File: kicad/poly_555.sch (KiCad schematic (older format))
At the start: 32 parts, among them U1 LM386

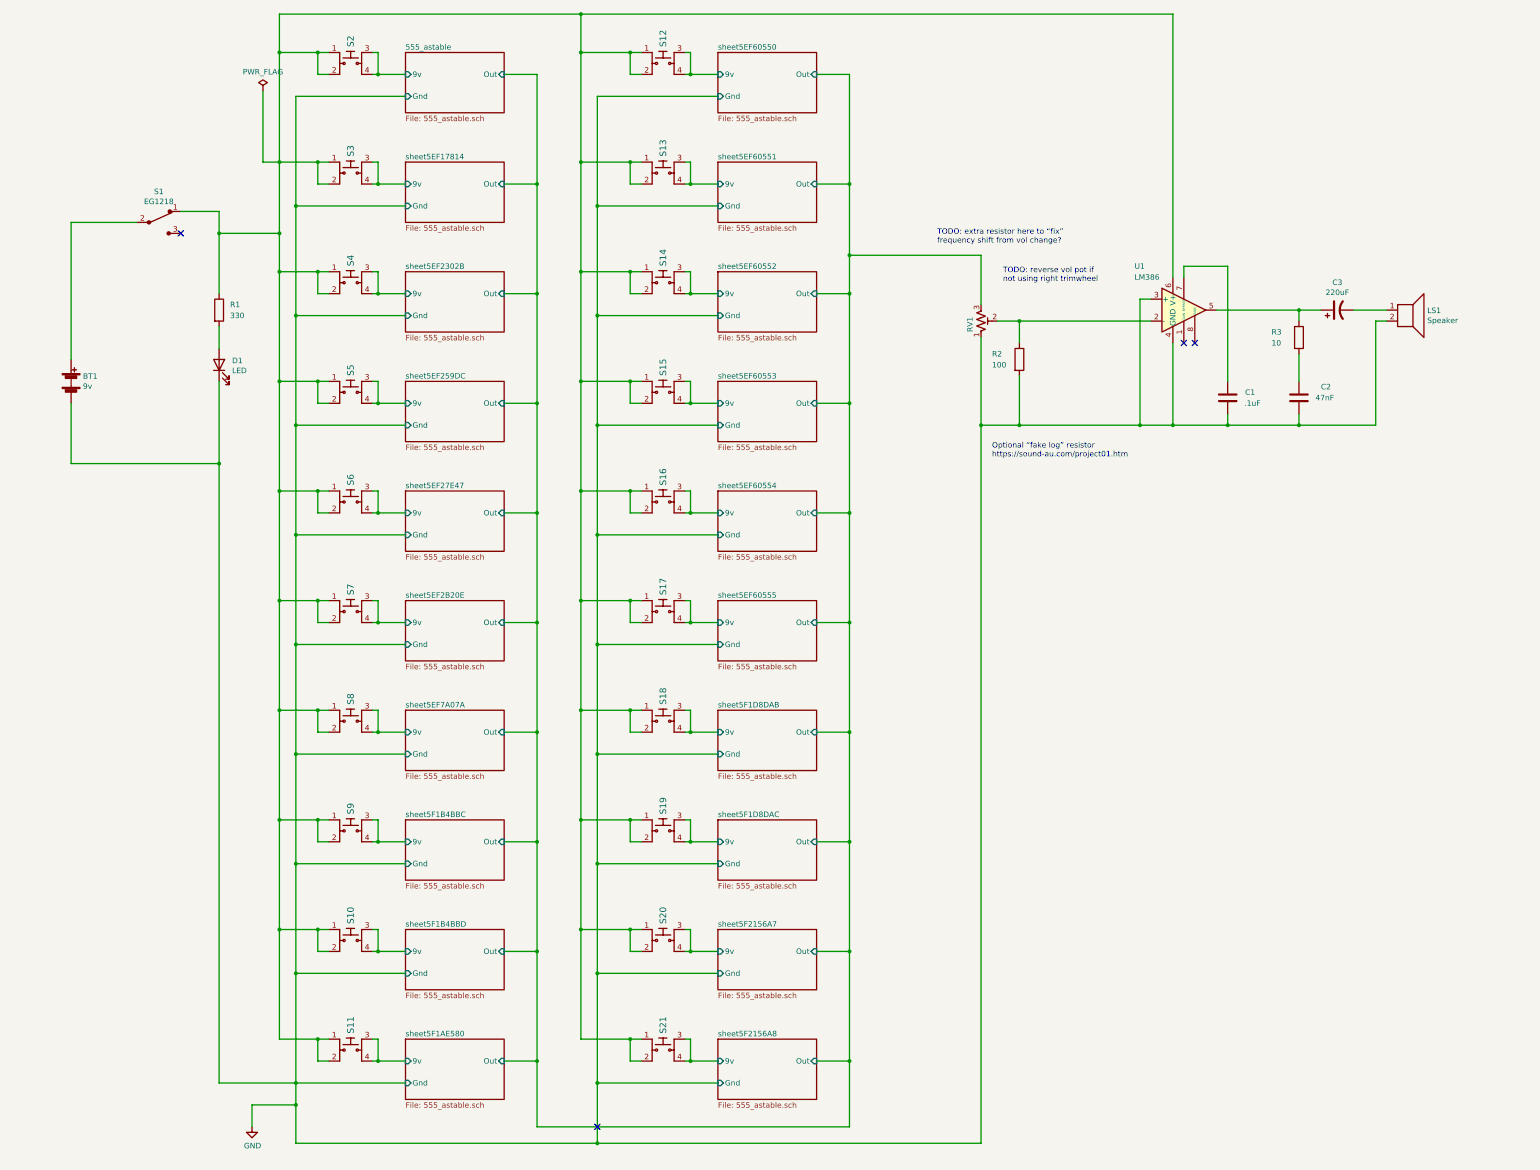
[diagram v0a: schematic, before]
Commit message: Re-annotate to fix key vs 555 mismatch
The alignment of switch to 555 circuit was off, starting around S8. I
believe this was from non-linear copy-pasting when key count jumped from
13 to 20.

No amound of fiddling with the annotation tool seemed to fix and to do
it manually was out of the question, so I ended up deleting 6-20 and
copy-pasting 1-5 three times. I think it worked...
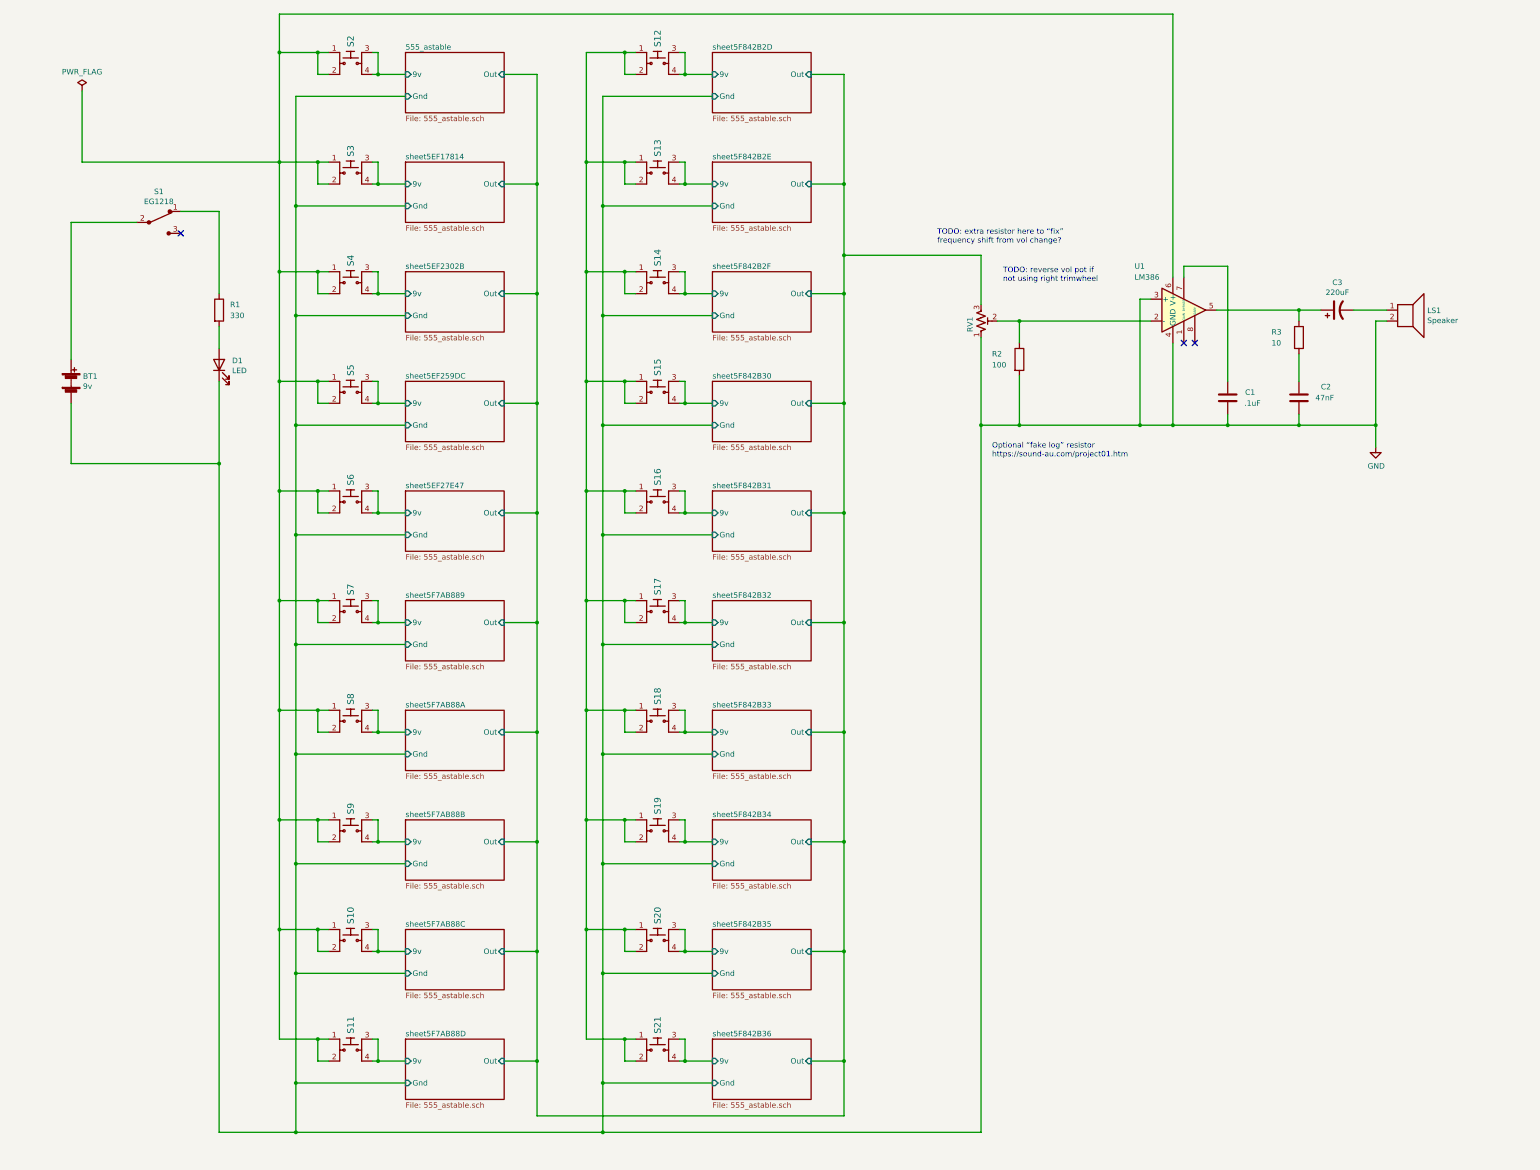
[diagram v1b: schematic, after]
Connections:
- net sheet5EF2B20E/9v renamed sheet5F7AB889/9v
- net sheet5EF60550/9v renamed sheet5F842B2D/9v
- net sheet5EF60551/9v renamed sheet5F842B2E/9v
- net sheet5EF60552/9v renamed sheet5F842B2F/9v
- net sheet5EF60553/9v renamed sheet5F842B30/9v
- net sheet5EF60554/9v renamed sheet5F842B31/9v
- net sheet5EF60555/9v renamed sheet5F842B32/9v
- net sheet5EF7A07A/9v renamed sheet5F7AB88A/9v
- net sheet5F1AE580/9v renamed sheet5F7AB88D/9v
- net sheet5F1B4BBC/9v renamed sheet5F7AB88B/9v
- net sheet5F1B4BBD/9v renamed sheet5F7AB88C/9v
- net sheet5F1D8DAB/9v renamed sheet5F842B33/9v
- net sheet5F1D8DAC/9v renamed sheet5F842B34/9v
- net sheet5F2156A7/9v renamed sheet5F842B35/9v
- net sheet5F2156A8/9v renamed sheet5F842B36/9v
- new net: S10.1, S10.2, S11.1, S11.2, S2.1, S2.2, S3.1, S3.2, S4.1, S4.2, S5.1, S5.2, S6.1, S6.2, S7.1, S7.2, S8.1, S8.2, S9.1, S9.2, U1.6 (V+)
- new net: R1.1, S1.1
- new net: S12.1, S12.2, S13.1, S13.2, S14.1, S14.2, S15.1, S15.2, S16.1, S16.2, S17.1, S17.2, S18.1, S18.2, S19.1, S19.2, S20.1, S20.2, S21.1, S21.2
- no-connect marks 4 -> 3

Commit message: Finish routing
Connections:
- net at S10.1, S10.2, S11.1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: now also R1.1, S1.1, S12.1, S12.2, S13.1, S13.2, S14.1, S14.2, S15.1, S15.2, S16.1, S16.2, S17.1, S17.2, S18.1, S18.2, S19.1, S19.2, S20.1, S20.2, S21.1, S21.2
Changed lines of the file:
@@
 	13100 4650 13100 4450
 Wire Wire Line
-	3100 700  11250 700
+	3100 700  5900 700
 $Sheet
 S 4250 6050 900  550
@@
 	2550 2500 2550 3250
 Wire Wire Line
-	3100 2050 3100 3050
+	3100 2050 3100 2500
 $Sheet
 S 7050 1050 900  550
@@
 Wire Wire Line
 	11250 4450 11750 4450
+Wire Wire Line
+	5900 700  5900 1050
+Connection ~ 5900 700
+Wire Wire Line
+	5900 700  11250 700
+Connection ~ 5900 1050
+Wire Wire Line
+	2550 2500 3100 2500
+Connection ~ 2550 2500
+Connection ~ 3100 2500
+Wire Wire Line
+	3100 2500 3100 3050
 $EndSCHEMATC

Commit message: Start new PCB layout
* wider cavity w/o top
* swap fine trimmer for resistor
* bigger wire holes for speaker,battery
* 5mm LEDs
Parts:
- D1: footprint LED_THT:LED_D3.0mm -> LED_THT:LED_D5.0mm
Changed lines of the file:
@@
 F 0 "D1" V 2589 3782 50  0000 R CNN
 F 1 "LED" V 2498 3782 50  0000 R CNN
-F 2 "LED_THT:LED_D3.0mm" H 2550 3900 50  0001 C CNN
+F 2 "LED_THT:LED_D5.0mm" H 2550 3900 50  0001 C CNN
 F 3 "~" H 2550 3900 50  0001 C CNN
 	1    2550 3900

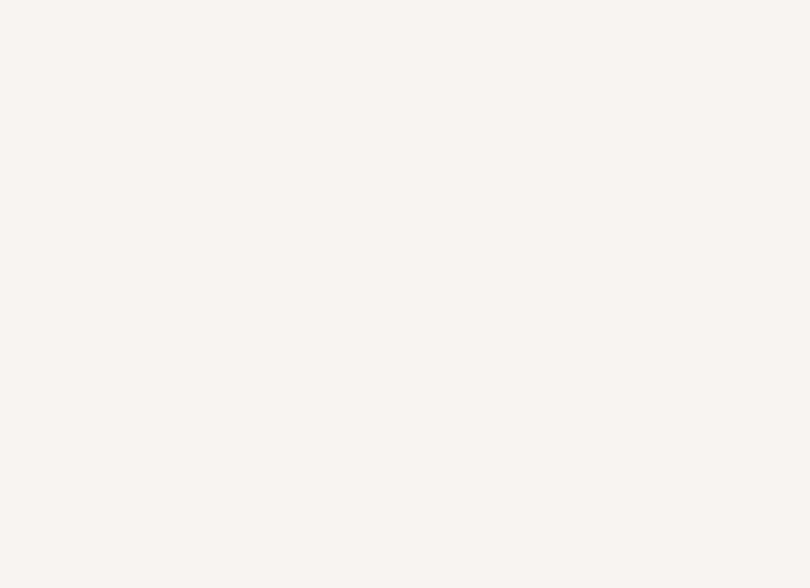
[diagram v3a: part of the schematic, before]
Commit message: Fill negative space with breakoff APC
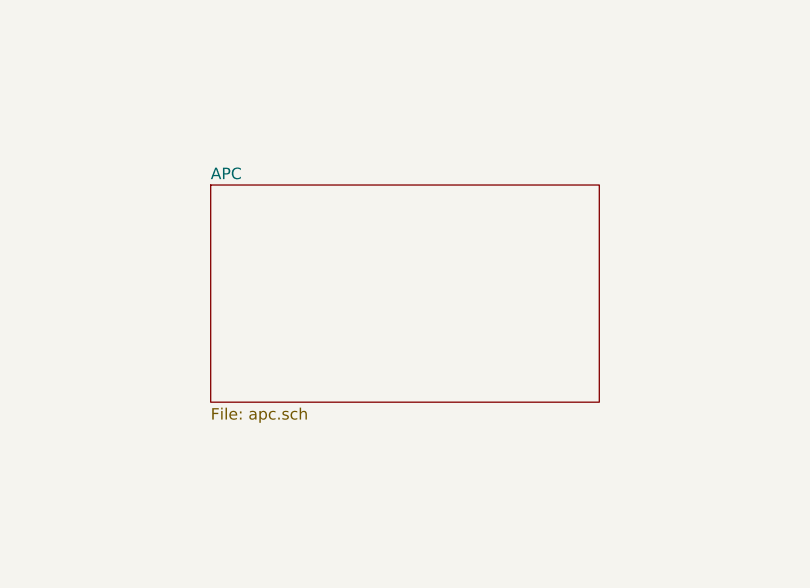
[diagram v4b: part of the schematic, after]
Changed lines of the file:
@@
 $Descr A3 16535 11693
 encoding utf-8
-Sheet 1 21
+Sheet 1 22
 Title ""
 Date ""
@@
 Wire Wire Line
 	3100 2500 3100 3050
+$Sheet
+S 10500 5850 1700 950
+U 5F470266
+F0 "APC" 50
+F1 "apc.sch" 50
+$EndSheet
 $EndSCHEMATC

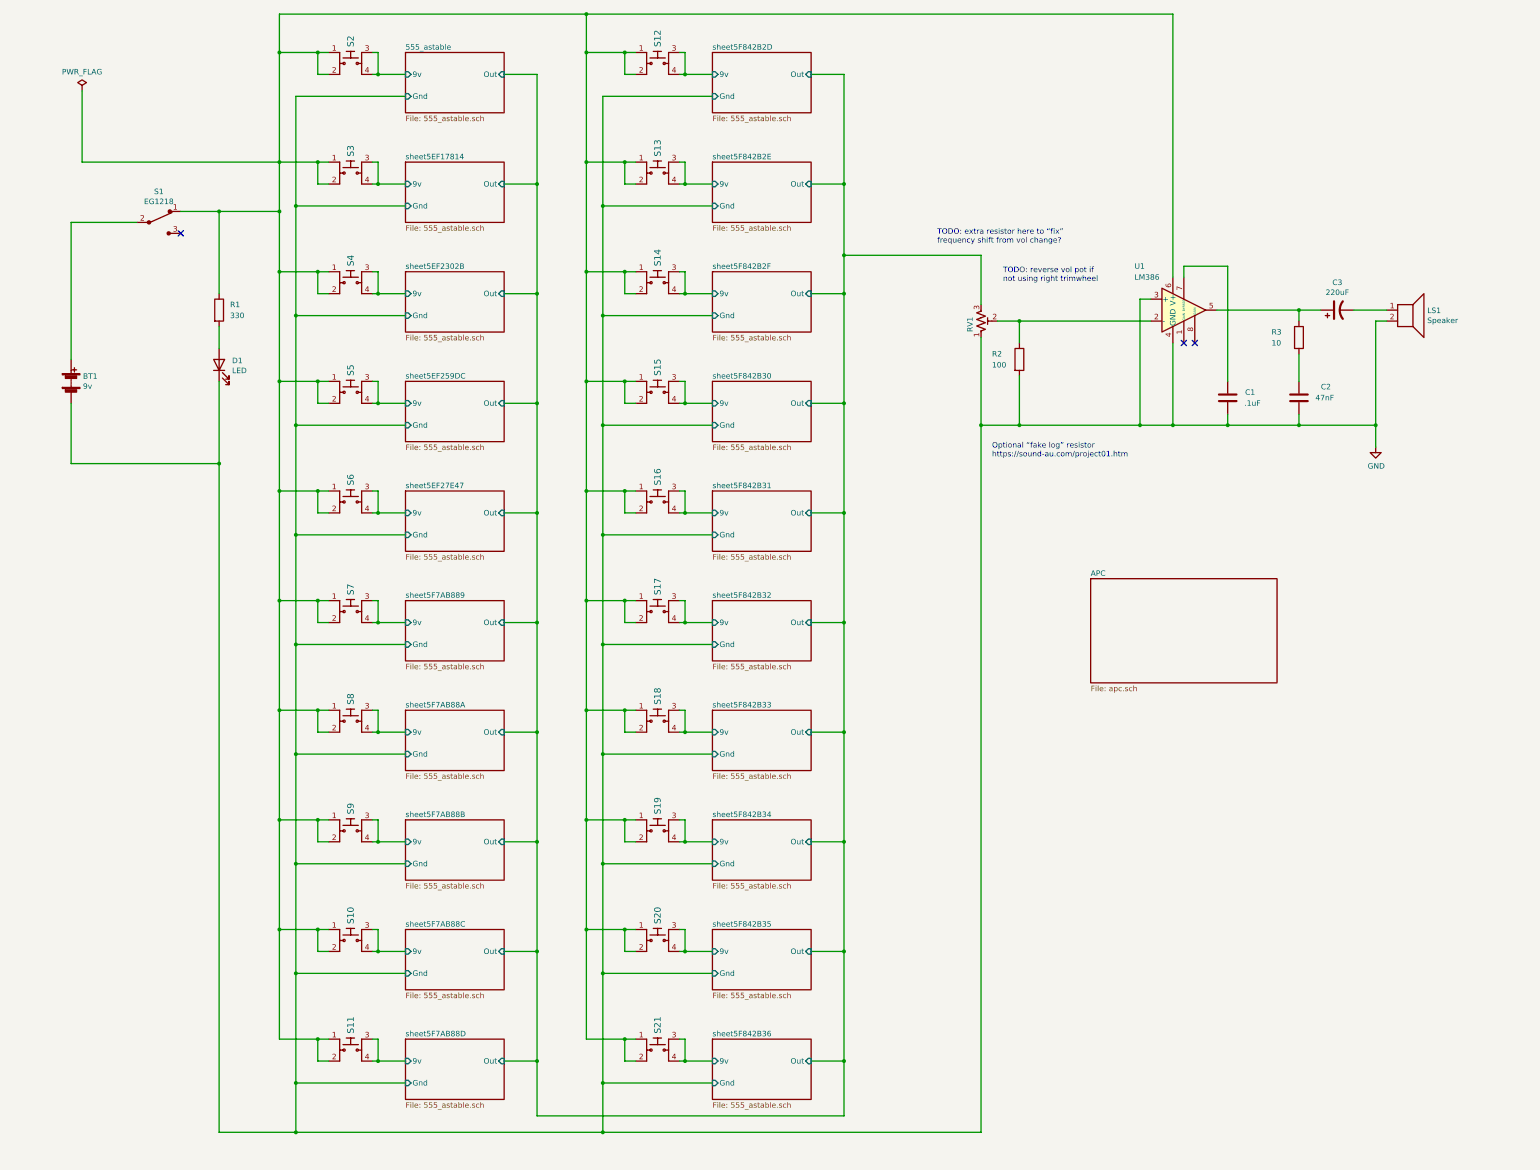
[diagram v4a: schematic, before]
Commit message: PCB revisions:
* Add voltage regulator to POLY_555
* Ditch hitch
* Reorder switches+circuits left to right
* Carve out room for battery
* Mark # 555s
* Label wired pins better

APC updates:

* Fix ground error
* Reverse volume pot direction
* Swap timing cap footprint
* Add stress relief hole for battery wires
* Widen speaker pins
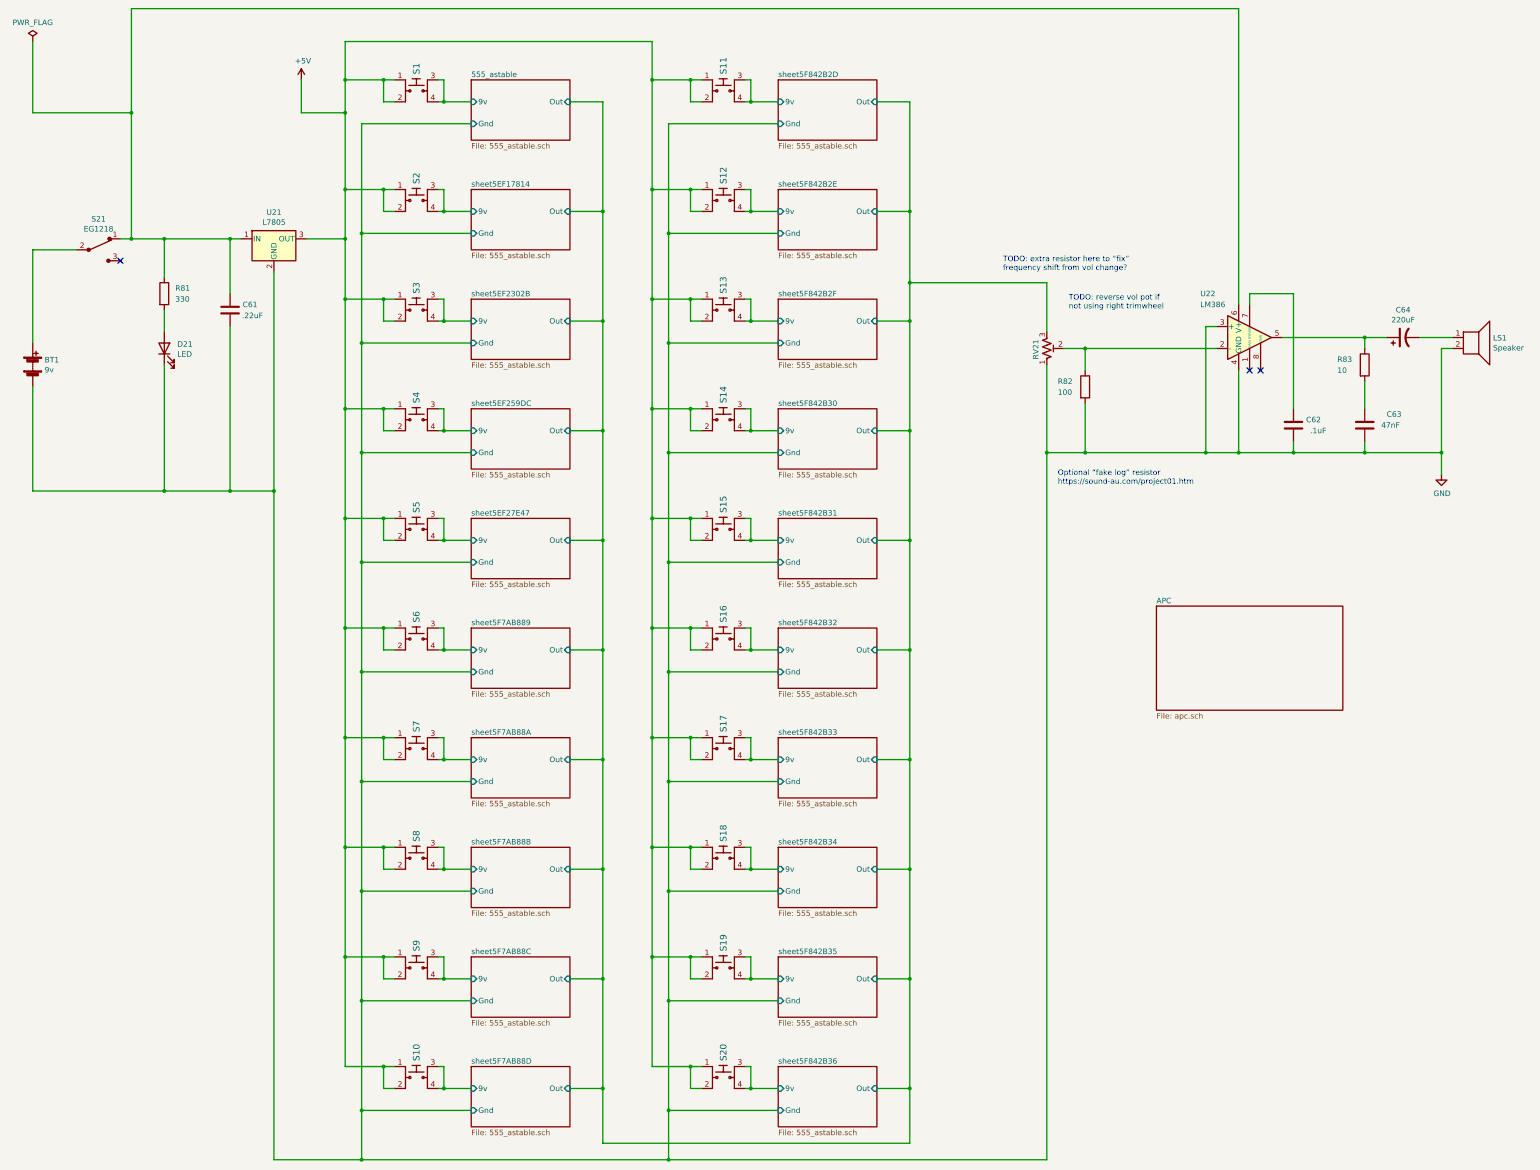
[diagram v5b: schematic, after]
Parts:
- removed C1: .1uF, Capacitor_THT:C_Disc_D5.0mm_W2.5mm_P5.00mm, symbol Device:C
- removed C2: 47nF, Capacitor_THT:C_Disc_D5.0mm_W2.5mm_P5.00mm, symbol Device:C
- removed C3: 220uF, Capacitor_THT:CP_Radial_D8.0mm_P3.50mm, symbol Device:CP1
- removed D1: LED, LED_THT:LED_D5.0mm, symbol Device:LED
- removed R1: 330, Resistor_THT:R_Axial_DIN0207_L6.3mm_D2.5mm_P2.54mm_Vertical, symbol Device:R
- removed R2: 100, Resistor_THT:R_Axial_DIN0207_L6.3mm_D2.5mm_P10.16mm_Horizontal, symbol Device:R
- removed R3: 10, Resistor_THT:R_Axial_DIN0207_L6.3mm_D2.5mm_P2.54mm_Vertical, symbol Device:R
- removed RV1: R_POT_TRIM_US, Potentiometer_THT:Potentiometer_Piher_PT-6-V_Vertical, symbol Device:R_POT_TRIM_US
- removed S1: EG1218, Button_Switch_THT:SW_Slide_1P2T_CK_OS102011MS2Q, symbol dk_Slide-Switches:EG1218
- removed U1: LM386, Package_DIP:DIP-8_W7.62mm, symbol Amplifier_Audio:LM386
- added C61: .22uF, Capacitor_THT:C_Disc_D5.0mm_W2.5mm_P5.00mm, symbol Device:C
- added C62: .1uF, Capacitor_THT:C_Disc_D5.0mm_W2.5mm_P5.00mm, symbol Device:C
- added C63: 47nF, Capacitor_THT:C_Disc_D5.0mm_W2.5mm_P5.00mm, symbol Device:C
- added C64: 220uF, Capacitor_THT:CP_Radial_D8.0mm_P3.50mm, symbol Device:CP1
- added D21: LED, LED_THT:LED_D5.0mm, symbol Device:LED
- added R81: 330, Resistor_THT:R_Axial_DIN0207_L6.3mm_D2.5mm_P2.54mm_Vertical, symbol Device:R
- added R82: 100, Resistor_THT:R_Axial_DIN0207_L6.3mm_D2.5mm_P10.16mm_Horizontal, symbol Device:R
- added R83: 10, Resistor_THT:R_Axial_DIN0207_L6.3mm_D2.5mm_P2.54mm_Vertical, symbol Device:R
- added RV21: R_POT_TRIM_US, Potentiometer_THT:Potentiometer_Piher_PT-6-V_Vertical, symbol Device:R_POT_TRIM_US
- added S21: EG1218, Button_Switch_THT:SW_Slide_1P2T_CK_OS102011MS2Q, symbol dk_Slide-Switches:EG1218
- added U21: L7805, Package_TO_SOT_THT:TO-220F-3_Horizontal_TabDown, symbol Regulator_Linear:L7805
- added U22: LM386, Package_DIP:DIP-8_W7.62mm, symbol Amplifier_Audio:LM386
- renumbered S2 to S1, S11 to S10, S12 to S11, S13 to S12, S14 to S13, S15 to S14, S16 to S15, S17 to S16, S18 to S17, S19 to S18, S20 to S19, S3 to S2, S21 to S20, S4 to S3, S5 to S4, S6 to S5, S7 to S6, S8 to S7, S9 to S8, S10 to S9
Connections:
- net 555_astable/Out: now also RV21.3
- net GND: now also C61.1, C62.1, C63.2, D21.1 (K), R82.2, RV21.1, U21.2 (GND), U22.3 (+), U22.4 (GND)
- net at BT1.1 (+): now also S21.2
- net +5V: now reaches S1.1, S1.2, S10.1, S10.2, S11.1, S11.2, S12.1, S12.2, S13.1, S13.2, S14.1, S14.2, S15.1, S15.2, S16.1, S16.2, S17.1, S17.2, S18.1, S18.2, S19.1, S19.2, S2.1, S2.2, S20.1, S20.2, S3.1, S3.2, S4.1, S4.2, S5.1, S5.2, S6.1, S6.2, S7.1, S7.2, S8.1, S8.2, S9.1, S9.2
- net +5V: now also U21.3 (OUT)
- net at LS1.1: now also C64.2
- new net: D21.2 (A), R81.2
- new net: C61.2, R81.1, S21.1, U21.1 (IN), U22.6 (V+)
- new net: R82.1, RV21.2, U22.2 (-)
- new net: C63.1, R83.2
- new net: C64.1, R83.1, U22.5
- new net: C62.2, U22.7 (BYPASS)
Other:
- moved on the sheet: S1, S10, S11, S12, S13, S14, S15, S16, S17, S18, S19, S2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
